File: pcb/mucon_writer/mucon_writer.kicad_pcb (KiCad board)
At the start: 2 copper layers, 22 x 26 mm, 12 parts, among them IC1 NJM2866F33-TE1, J1 Conn_01x07, J2 Conn_01x04, J3 Conn_01x04, J4 Conn_02x05_Top_Bottom, J6 USB_C_Receptacle_USB2.0

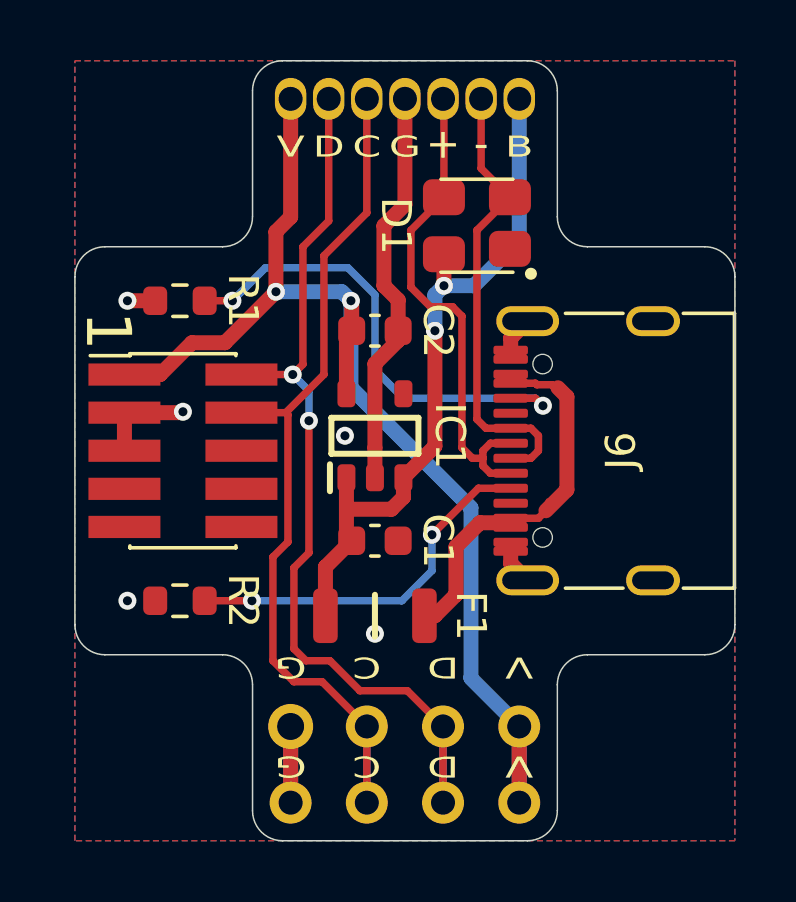
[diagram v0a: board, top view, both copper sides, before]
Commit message: change capacitor (from 1uF to 100uF), PCB design files are in KiCad6 format
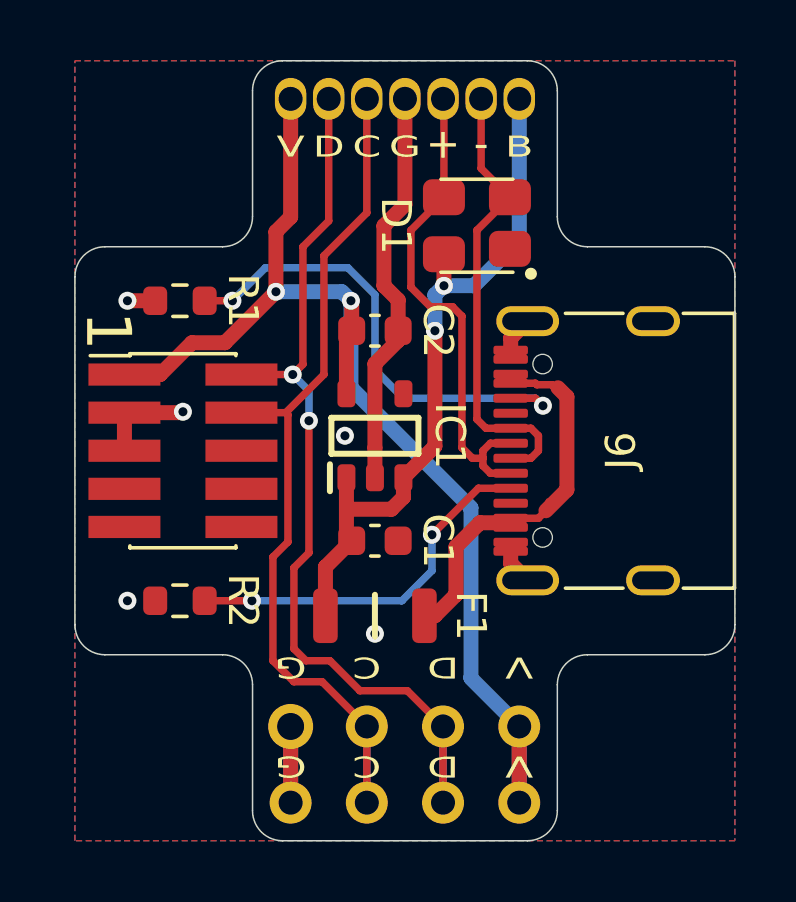
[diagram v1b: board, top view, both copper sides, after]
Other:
- net class Default removed
- net class Power removed
